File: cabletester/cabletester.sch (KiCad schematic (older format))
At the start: 26 parts, among them J1 IDC 2x5, J2 IDC 2x8, J3 IDC 2x5, J4 IDC 2x8, J5 4 pin header, J6 4 pin header, U1 4051

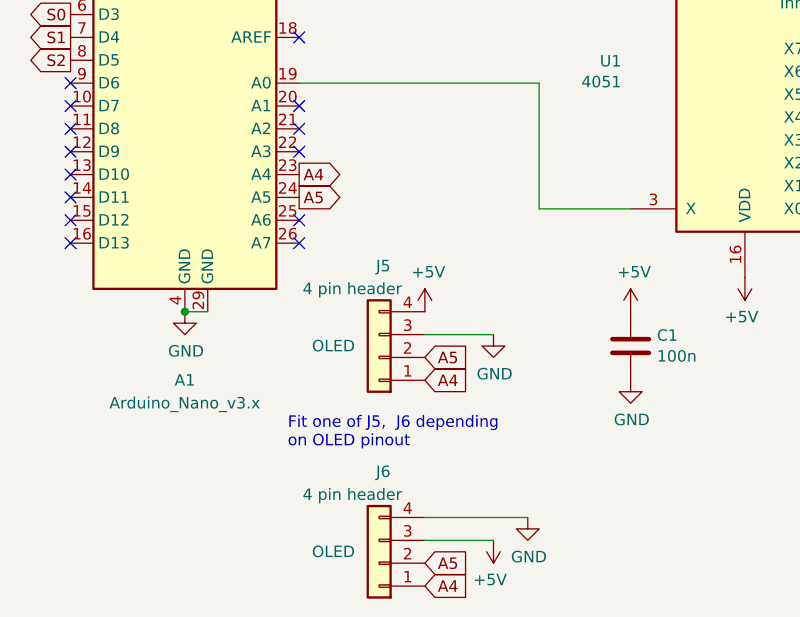
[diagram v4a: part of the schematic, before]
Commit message: Clearer labels; software revisions to match my woring
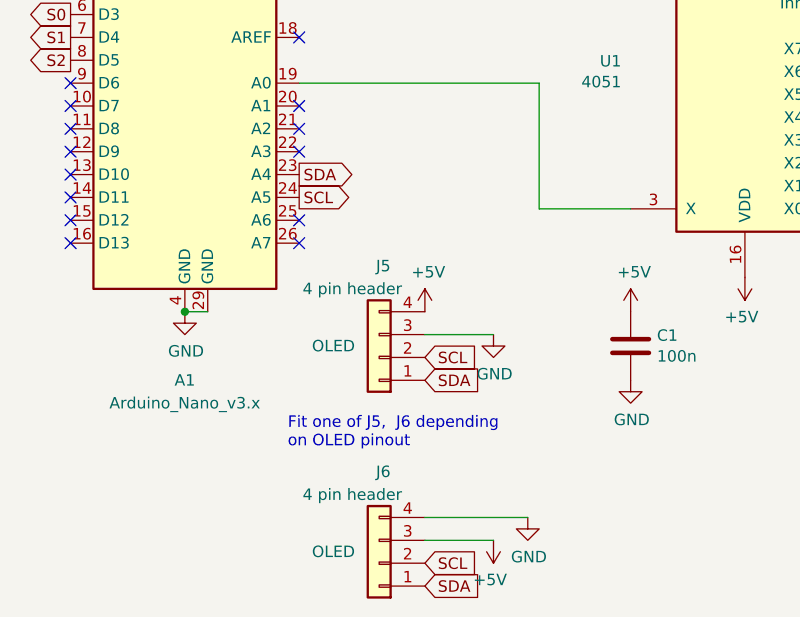
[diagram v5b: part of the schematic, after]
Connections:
- net A4 renamed SDA
- net A5 renamed SCL
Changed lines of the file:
@@
 	3350 5500 3650 5500
 Text GLabel 3350 5700 2    50   Input ~ 0
-A4
+SDA
 Text GLabel 3350 5600 2    50   Input ~ 0
-A5
+SCL
 Text GLabel 2800 4800 2    50   Output ~ 0
-A4
+SDA
 Text GLabel 2800 4900 2    50   Output ~ 0
-A5
+SCL
 Wire Wire Line
 	2400 5400 2300 5400
@@
 $EndComp
 Text GLabel 3350 6600 2    50   Input ~ 0
-A4
+SDA
 Text GLabel 3350 6500 2    50   Input ~ 0
-A5
+SCL
 $Comp
 L Connector_Generic:Conn_01x04 J6
